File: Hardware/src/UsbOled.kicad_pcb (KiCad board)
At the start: 2 copper layers, 27.4 x 12 mm, 13 parts, among them J1 ‎USB4085, U1 16F1454

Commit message: Added optional I2C pull-up resistors
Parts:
- added R4: 5K1, Medo64:R Optional (0805), B.Cu at (33.8, 21.0)
- added R5: 5K1, Medo64:R Optional (0805), B.Cu at (36.2, 21.0)
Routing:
- net 5V: track 42.1 -> 45.9 mm
- net OLED_SDA: track 7.36 -> 10.9 mm
- net OLED_SCL: track 15.4 -> 18.8 mm
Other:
- board text added: "PULL-UP"
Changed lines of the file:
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@@
         (effects (font (size 0.8 0.6) (thickness 0.15)))
     )
-    (fp_text value "5K1" (at -2.3 -2.6 90) (layer "F.SilkS")
+    (fp_text value "5K1" (at -2.3 0 90) (layer "F.SilkS")
         (effects (font (size 0.8 0.6) (thickness 0.15)))
     )
@@
         (effects (font (size 0.8 0.6) (thickness 0.15)))
     )
-    (fp_text value "5K1" (at -2.3 2.75 270) (layer "F.SilkS")
+    (fp_text value "5K1" (at -2.3 0 270) (layer "F.SilkS")
         (effects (font (size 0.8 0.6) (thickness 0.15)))
     )
@@
       (stroke (width 0.1) (type solid)) (fill solid) (layer "B.Mask"))
   )
+  (footprint "Medo64:R Optional (0805)" (layer "B.Cu")
+    (at 36.25 21 -90)
+    (tags "RESC2013X70N")
+    (attr smd exclude_from_bom)
+    (fp_text reference "R5" (at 0 1.6 90) (layer "B.SilkS") hide
+        (effects (font (size 0.8 0.6) (thickness 0.15)) (justify mirror))
+    )
+    (fp_text value "5K1" (at 0 -1.7 90) (layer "B.SilkS") hide
+        (effects (font (size 0.8 0.6) (thickness 0.15)) (justify mirror))
+    )
+    (fp_line (start -0.25 -0.6) (end 0.25 -0.6)
+      (stroke (width 0.2) (type default)) (layer "B.SilkS"))
+    (fp_line (start -0.25 0.6) (end 0.25 0.6)
+      (stroke (width 0.2) (type default)) (layer "B.SilkS"))
+    (fp_rect (start -1.65 0.85) (end 1.65 -0.85)
+      (stroke (width 0.2) (type dash)) (fill none) (layer "B.SilkS"))
+    (fp_rect (start -1.75 0.95) (end 1.75 -0.95)
+      (stroke (width 0.01) (type dash)) (fill none) (layer "B.CrtYd"))
+    (fp_rect (start -1 0.625) (end 1 -0.625)
+      (stroke (width 0.01) (type dash_dot)) (fill none) (layer "B.Fab"))
+    (pad "1" smd roundrect (at -0.95 0 270) (size 1.05 1.4) (layers "B.Cu" "B.Mask") (roundrect_rratio 0.25)
+      (net 2 "OLED_SDA") (thermal_bridge_angle 45))
+    (pad "2" smd roundrect (at 0.95 0 270) (size 1.05 1.4) (layers "B.Cu" "B.Mask") (roundrect_rratio 0.25)
+      (net 3 "5V") (thermal_bridge_angle 45))
+  )
+  (footprint "Medo64:R Optional (0805)" (layer "B.Cu")
+    (at 33.75 21 -90)
+    (tags "RESC2013X70N")
+    (attr smd exclude_from_bom)
+    (fp_text reference "R4" (at 0 1.6 90) (layer "B.SilkS") hide
+        (effects (font (size 0.8 0.6) (thickness 0.15)) (justify mirror))
+    )
+    (fp_text value "5K1" (at 0 -1.7 90) (layer "B.SilkS") hide
+        (effects (font (size 0.8 0.6) (thickness 0.15)) (justify mirror))
+    )
+    (fp_line (start -0.25 -0.6) (end 0.25 -0.6)
+      (stroke (width 0.2) (type default)) (layer "B.SilkS"))
+    (fp_line (start -0.25 0.6) (end 0.25 0.6)
+      (stroke (width 0.2) (type default)) (layer "B.SilkS"))
+    (fp_rect (start -1.65 0.85) (end 1.65 -0.85)
+      (stroke (width 0.2) (type dash)) (fill none) (layer "B.SilkS"))
+    (fp_rect (start -1.75 0.95) (end 1.75 -0.95)
+      (stroke (width 0.01) (type dash)) (fill none) (layer "B.CrtYd"))
+    (fp_rect (start -1 0.625) (end 1 -0.625)
+      (stroke (width 0.01) (type dash_dot)) (fill none) (layer "B.Fab"))
+    (pad "1" smd roundrect (at -0.95 0 270) (size 1.05 1.4) (layers "B.Cu" "B.Mask") (roundrect_rratio 0.25)
+      (net 1 "OLED_SCL") (thermal_bridge_angle 45))
+    (pad "2" smd roundrect (at 0.95 0 270) (size 1.05 1.4) (layers "B.Cu" "B.Mask") (roundrect_rratio 0.25)
+      (net 3 "5V") (thermal_bridge_angle 45))
+  )
   (footprint "Medo64:DS OLED 128x32 SPI (4w)" (layer "B.Cu")
     (at 40.8 21 90)
@@
     (effects (font (size 0.8 0.6) (thickness 0.15) bold) (justify bottom mirror))
   )
+  (gr_text "PULL-UP" (at 35 23.8) (layer "B.SilkS")
+    (effects (font (size 0.8 0.6) (thickness 0.15) bold) (justify bottom mirror))
+  )
   (gr_text "UsbOled B" (at 31.2 18.2) (layer "B.SilkS")
     (effects (font (size 0.8 0.6) (thickness 0.15) bold) (justify top mirror))
@@
   (segment (start 40.805635 15.6) (end 41.9 16.694365) (width 0.2) (layer "F.Cu") (net 1))
   (segment (start 35.45 15.6) (end 40.805635 15.6) (width 0.2) (layer "F.Cu") (net 1))
+  (segment (start 33.74 16.6) (end 33.74 19.99) (width 0.2) (layer "B.Cu") (net 1))
+  (segment (start 33.74 19.99) (end 33.8 20.05) (width 0.2) (layer "B.Cu") (net 1))
   (segment (start 35.86 17.08) (end 36.34 16.6) (width 0.2) (layer "F.Cu") (net 2))
   (segment (start 40 16.35) (end 40.84 17.19) (width 0.2) (layer "F.Cu") (net 2))
   (segment (start 35.86 19.1) (end 35.86 17.08) (width 0.2) (layer "F.Cu") (net 2))
   (segment (start 36.53 16.35) (end 40 16.35) (width 0.2) (layer "F.Cu") (net 2))
+  (segment (start 36.28 16.6) (end 36.28 19.77) (width 0.2) (layer "B.Cu") (net 2))
+  (segment (start 36.28 19.77) (end 36 20.05) (width 0.2) (layer "B.Cu") (net 2))
   (segment (start 31.7 24.9) (end 32.61 24.9) (width 0.2) (layer "F.Cu") (net 3))
   (segment (start 40.8 21.3) (end 38.6 19.1) (width 0.2) (layer "F.Cu") (net 3))
@@
   (segment (start 40.8 22.27) (end 41.9 21.17) (width 0.2) (layer "B.Cu") (net 3))
   (segment (start 41.9 16.734365) (end 40.765635 15.6) (width 0.2) (layer "B.Cu") (net 3))
-  (segment (start 32.2 24.4) (end 32.2 15.6) (width 0.2) (layer "B.Cu") (net 3))
+  (segment (start 36 21.95) (end 33.8 21.95) (width 0.2) (layer "B.Cu") (net 3))
+  (segment (start 32.25 21.95) (end 32.2 22) (width 0.2) (layer "B.Cu") (net 3))
   (segment (start 31.7 24.9) (end 32.2 24.4) (width 0.2) (layer "B.Cu") (net 3))
   (segment (start 29.66 15.6) (end 28.66 16.6) (width 0.2) (layer "B.Cu") (net 3))
+  (segment (start 32.2 24.4) (end 32.2 22) (width 0.2) (layer "B.Cu") (net 3))
   (segment (start 40.765635 15.6) (end 29.66 15.6) (width 0.2) (layer "B.Cu") (net 3))
+  (segment (start 32.2 22) (end 32.2 15.6) (width 0.2) (layer "B.Cu") (net 3))
   (segment (start 41.9 21.17) (end 41.9 16.734365) (width 0.2) (layer "B.Cu") (net 3))
+  (segment (start 33.8 21.95) (end 32.25 21.95) (width 0.2) (layer "B.Cu") (net 3))
   (segment (start 27.51 23.15) (end 26.56 24.1) (width 0.2) (layer "F.Cu") (net 4))
   (segment (start 26.56 26.205495) (end 26.56 26.3) (width 0.2) (layer "F.Cu") (net 4))

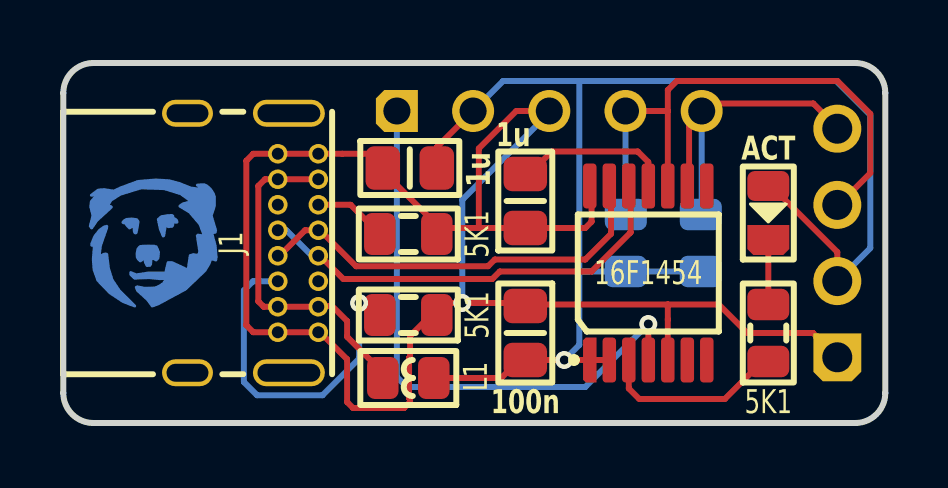
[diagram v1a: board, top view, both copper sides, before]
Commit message: Refactored I2C pullups to use 3V3 line
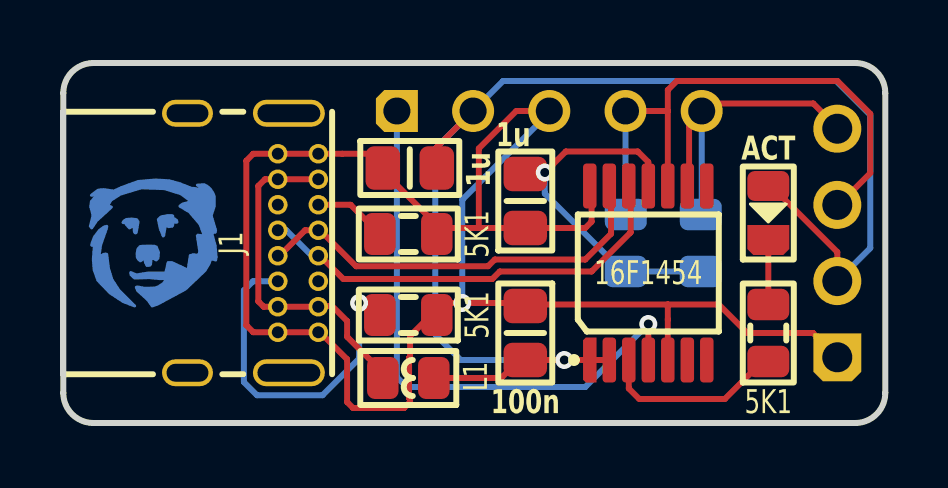
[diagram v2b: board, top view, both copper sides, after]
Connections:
- R4 pad 2: 5V -> 3V3
- R5 pad 2: 5V -> 3V3
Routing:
- net 3V3: track 4.95 -> 12.9 mm, vias 0 -> 1
- net 5V: track 45.9 -> 45.2 mm
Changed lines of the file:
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@@
       (net 2 "OLED_SDA") (thermal_bridge_angle 45))
     (pad "2" smd roundrect (at 0.95 0 270) (size 1.05 1.4) (layers "B.Cu" "B.Mask") (roundrect_rratio 0.25)
-      (net 3 "5V") (thermal_bridge_angle 45))
+      (net 6 "3V3") (thermal_bridge_angle 45))
   )
   (footprint "Medo64:R Optional (0805)" (layer "B.Cu")
@@
       (net 1 "OLED_SCL") (thermal_bridge_angle 45))
     (pad "2" smd roundrect (at 0.95 0 270) (size 1.05 1.4) (layers "B.Cu" "B.Mask") (roundrect_rratio 0.25)
-      (net 3 "5V") (thermal_bridge_angle 45))
+      (net 6 "3V3") (thermal_bridge_angle 45))
   )
   (footprint "Medo64:DS OLED 128x32 SPI (4w)" (layer "B.Cu")
@@
     (effects (font (size 0.8 0.6) (thickness 0.15) bold) (justify bottom mirror))
   )
-  (gr_text "UsbOled B" (at 31.2 18.2) (layer "B.SilkS")
-    (effects (font (size 0.8 0.6) (thickness 0.15) bold) (justify top mirror))
+  (gr_text "UsbOled B" (at 31.2 26.5) (layer "B.SilkS")
+    (effects (font (size 0.8 0.6) (thickness 0.15) bold) (justify bottom mirror))
   )
   (gr_text "GND" (at 38.2 24.8 270) (layer "B.SilkS")
@@
   (segment (start 40.8 22.27) (end 41.9 21.17) (width 0.2) (layer "B.Cu") (net 3))
   (segment (start 41.9 16.734365) (end 40.765635 15.6) (width 0.2) (layer "B.Cu") (net 3))
-  (segment (start 36 21.95) (end 33.8 21.95) (width 0.2) (layer "B.Cu") (net 3))
-  (segment (start 32.25 21.95) (end 32.2 22) (width 0.2) (layer "B.Cu") (net 3))
-  (segment (start 31.7 24.9) (end 32.2 24.4) (width 0.2) (layer "B.Cu") (net 3))
+  (segment (start 27.4 17.86) (end 27.4 24.05) (width 0.2) (layer "B.Cu") (net 3))
+  (segment (start 31.7 24.9) (end 28.25 24.9) (width 0.2) (layer "B.Cu") (net 3))
+  (segment (start 28.66 16.6) (end 27.4 17.86) (width 0.2) (layer "B.Cu") (net 3))
+  (segment (start 28.25 24.9) (end 27.4 24.05) (width 0.2) (layer "B.Cu") (net 3))
   (segment (start 29.66 15.6) (end 28.66 16.6) (width 0.2) (layer "B.Cu") (net 3))
-  (segment (start 32.2 24.4) (end 32.2 22) (width 0.2) (layer "B.Cu") (net 3))
   (segment (start 40.765635 15.6) (end 29.66 15.6) (width 0.2) (layer "B.Cu") (net 3))
-  (segment (start 32.2 22) (end 32.2 15.6) (width 0.2) (layer "B.Cu") (net 3))
   (segment (start 41.9 21.17) (end 41.9 16.734365) (width 0.2) (layer "B.Cu") (net 3))
-  (segment (start 33.8 21.95) (end 32.25 21.95) (width 0.2) (layer "B.Cu") (net 3))
   (segment (start 27.51 23.15) (end 26.56 24.1) (width 0.2) (layer "F.Cu") (net 4))
   (segment (start 26.56 26.205495) (end 26.56 26.3) (width 0.2) (layer "F.Cu") (net 4))
@@
   (segment (start 21.725 18.875) (end 23.56 18.875) (width 0.2) (layer "F.Cu") (net 5))
   (segment (start 21.5 22.945) (end 21.5 19.1) (width 0.2) (layer "F.Cu") (net 5))
-  (segment (start 34.15 17.95) (end 31.284314 17.95) (width 0.2) (layer "F.Cu") (net 6))
+  (segment (start 31.75 17.95) (end 31.05 18.65) (width 0.2) (layer "F.Cu") (net 6))
+  (segment (start 31.2 18.7) (end 31.294314 18.605686) (width 0.2) (layer "F.Cu") (net 6))
   (segment (start 34.5 18.3) (end 34.15 17.95) (width 0.2) (layer "F.Cu") (net 6))
-  (segment (start 30.96 18.274314) (end 30.96 18.605686) (width 0.2) (layer "F.Cu") (net 6))
+  (segment (start 31.294314 18.605686) (end 30.96 18.605686) (width 0.2) (layer "F.Cu") (net 6))
+  (segment (start 30.4 18.7) (end 31.2 18.7) (width 0.2) (layer "F.Cu") (net 6))
+  (segment (start 34.15 17.95) (end 31.75 17.95) (width 0.2) (layer "F.Cu") (net 6))
   (segment (start 34.5 19.1) (end 34.5 18.3) (width 0.2) (layer "F.Cu") (net 6))
-  (segment (start 31.284314 17.95) (end 30.96 18.274314) (width 0.2) (layer "F.Cu") (net 6))
+  (via (at 31.05 18.65) (size 0.6) (drill 0.3) (layers "F.Cu" "B.Cu") (net 6))
+  (segment (start 33.65 21.95) (end 33.75 21.95) (width 0.2) (layer "B.Cu") (net 6))
+  (segment (start 31.05 18.65) (end 31.05 19.35) (width 0.2) (layer "B.Cu") (net 6))
+  (segment (start 36.25 21.95) (end 33.75 21.95) (width 0.2) (layer "B.Cu") (net 6))
+  (segment (start 31.05 19.35) (end 33.65 21.95) (width 0.2) (layer "B.Cu") (net 6))
   (segment (start 32.4 21.55) (end 29.384314 21.55) (width 0.2) (layer "F.Cu") (net 7))
   (segment (start 33.26 19.1) (end 33.26 20.69) (width 0.2) (layer "F.Cu") (net 7))
